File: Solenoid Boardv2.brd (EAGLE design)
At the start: 76.2 x 31.8 mm, 52 parts, among them Y2 ECS-80-S-4X

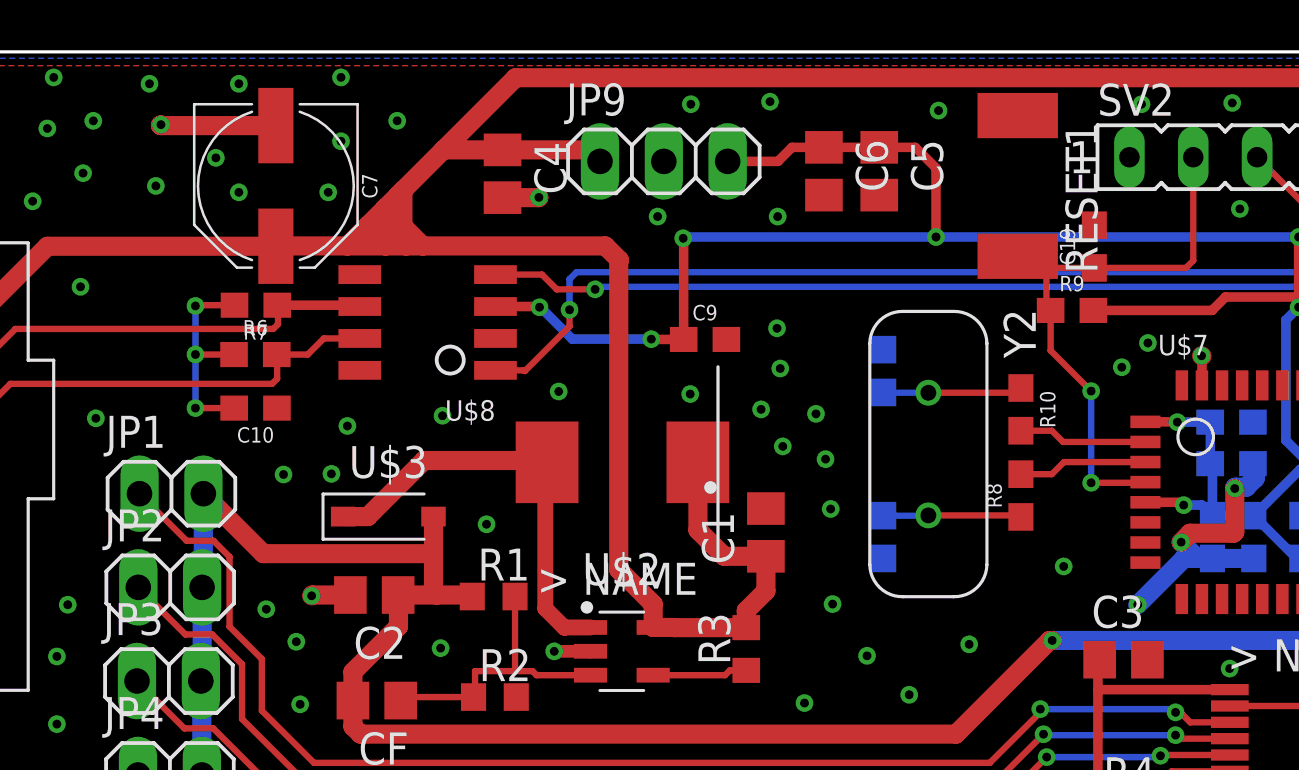
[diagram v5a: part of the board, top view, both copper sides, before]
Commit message: Moved nsrt around the osc signals
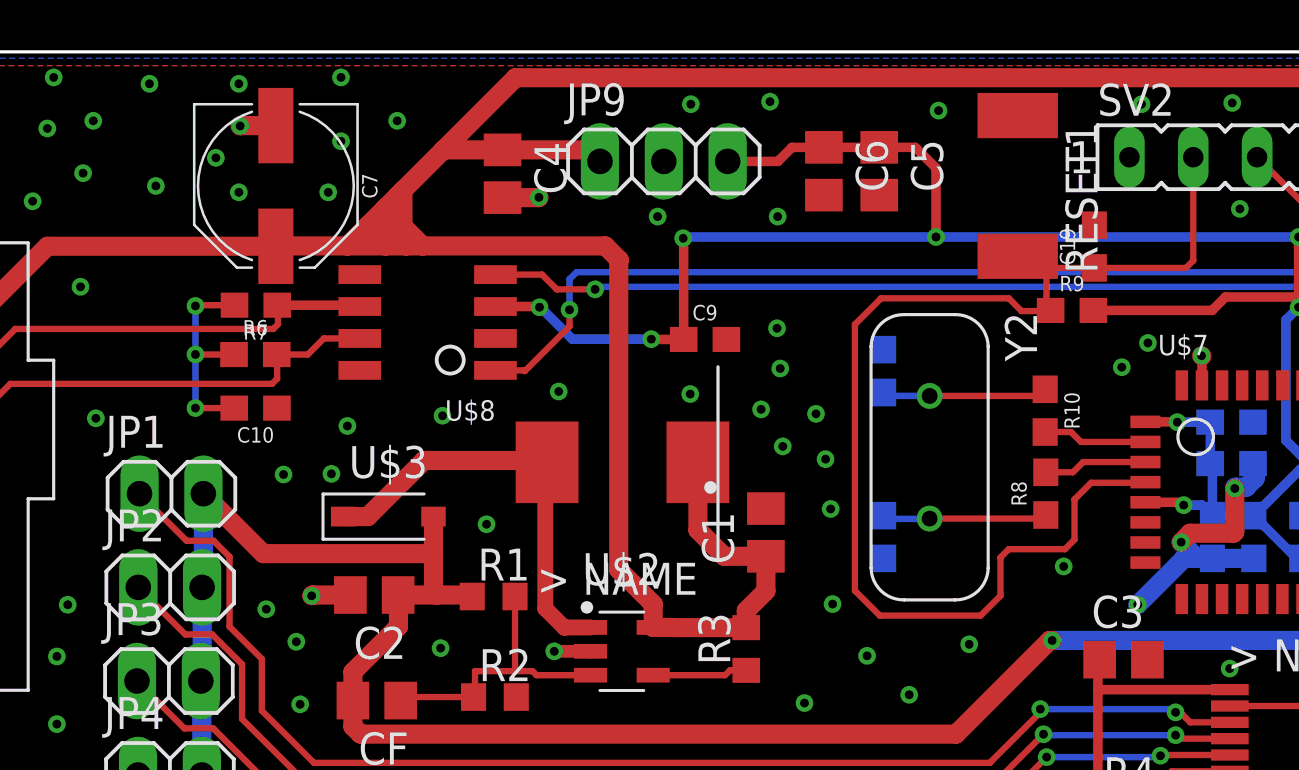
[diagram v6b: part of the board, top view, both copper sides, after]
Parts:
- moved R8 0.99 mm to (46.8, 14.2)
- moved R10 0.97 mm to (46.8, 17.5)
- moved Y2 0.14 mm to (42.2, 15.6)
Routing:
- net NRST: track 22.9 -> 48.2 mm, vias 2 -> 0
- net GND: track 27.5 -> 24.2 mm
- net N$3: track 5.49 -> 6.57 mm
- net N$4: track 5.54 -> 6.59 mm
- net OSC_OUT: track 5.15 -> 4.13 mm
- net OSC_IN: track 5.14 -> 4.15 mm

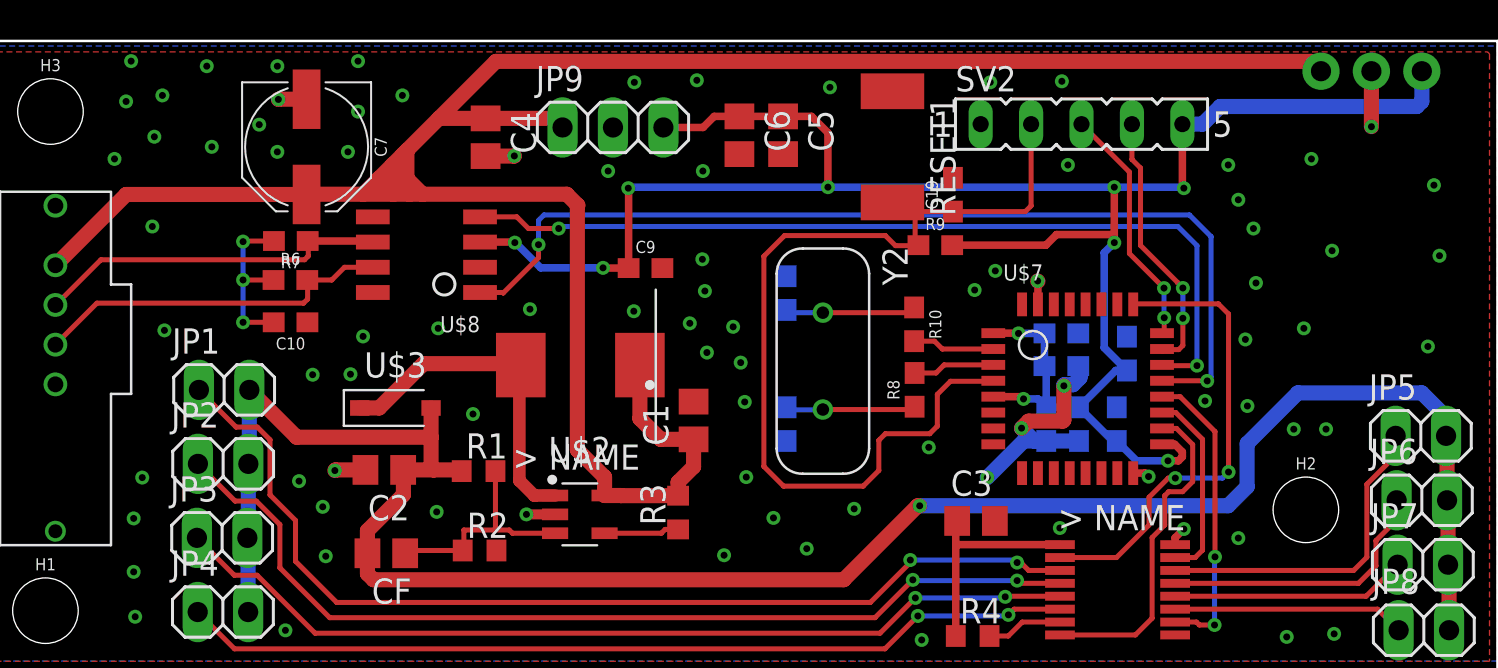
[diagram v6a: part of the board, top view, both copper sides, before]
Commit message: Fixed the via stitching
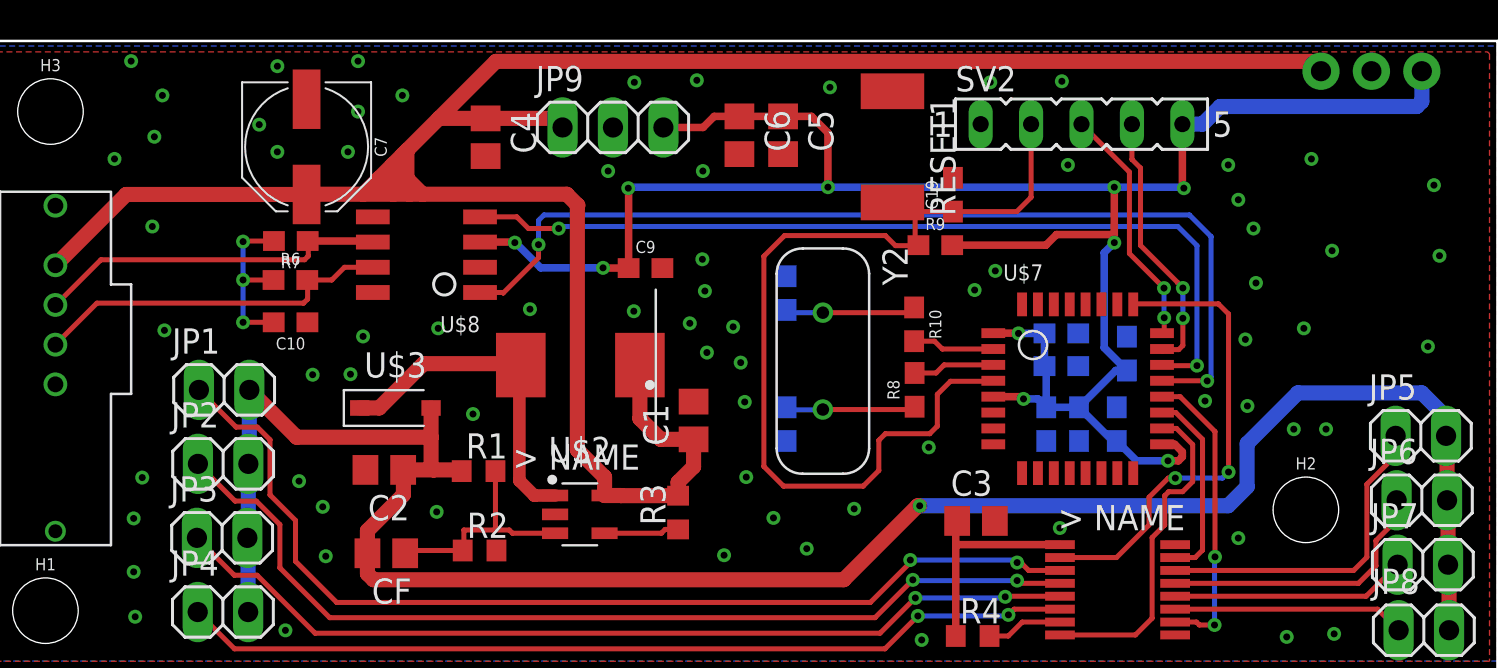
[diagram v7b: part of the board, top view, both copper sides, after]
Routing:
- net GND: track 24.2 -> 0.00 mm, vias 13 -> 71

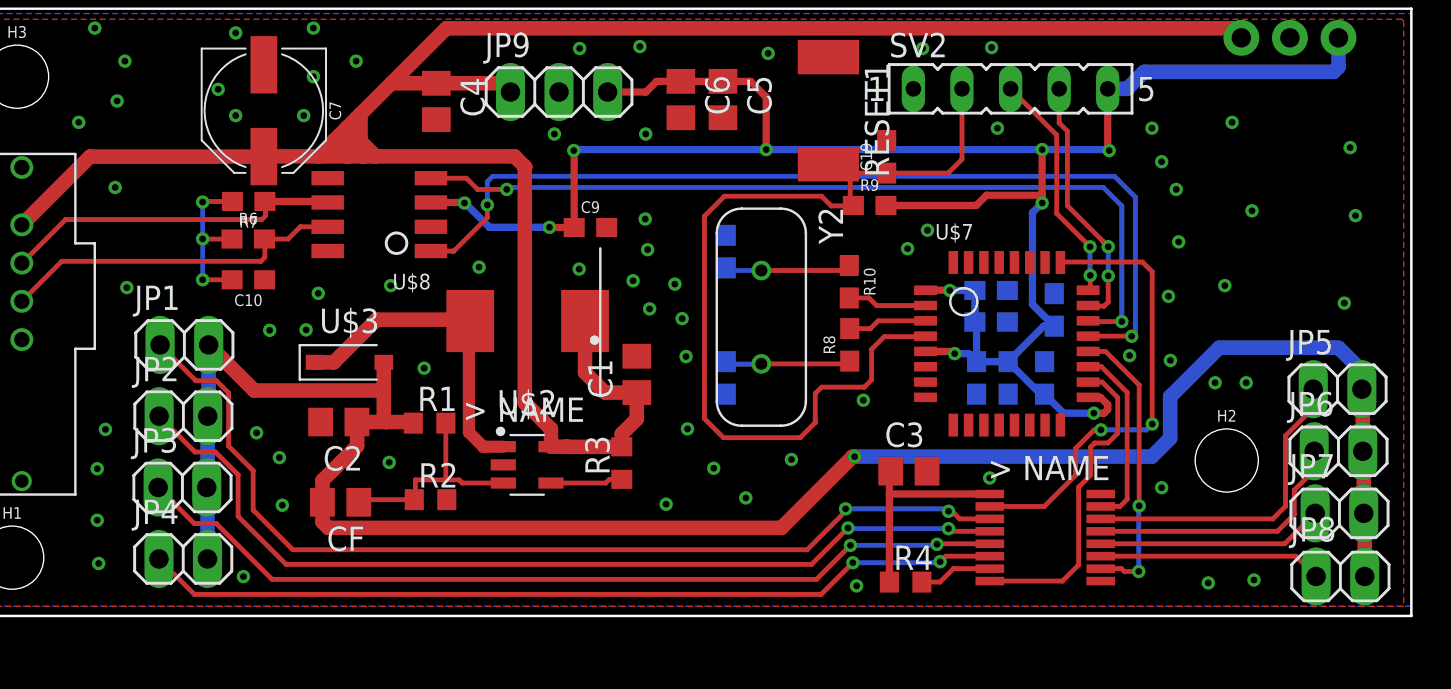
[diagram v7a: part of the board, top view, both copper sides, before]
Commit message: Fixed airwires and aligned the solenoid header pins
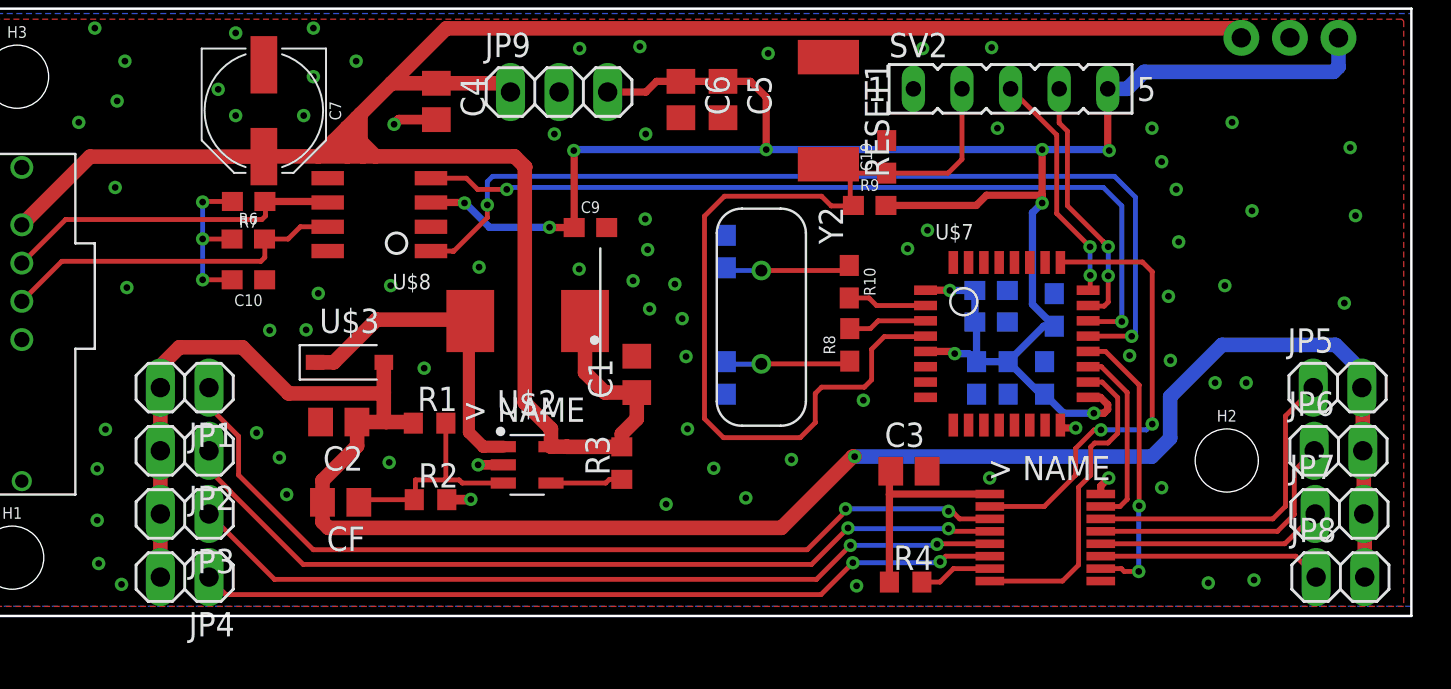
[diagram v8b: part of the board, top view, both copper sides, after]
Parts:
- moved JP1 2.23 mm to (12.1, 11.9), turned to 180 degrees
- moved JP2 1.81 mm to (12.1, 8.64), turned to 180 degrees
- moved JP3 1.39 mm to (12.1, 5.33), turned to 180 degrees
- moved JP4 0.95 mm to (12.1, 2.03), turned to 180 degrees
- moved JP5 0.08 mm to (72.3, 11.9)
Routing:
- net GND: track 0.00 -> 6.76 mm, vias 71 -> 76
- net DRAIN0: track 51.8 -> 47.3 mm
- net DRAIN1: track 48.8 -> 44.7 mm
- net DRAIN2: track 46.2 -> 43.0 mm
- net DRAIN3: track 45.0 -> 42.1 mm
- net +24V: track 104.5 -> 107.4 mm
